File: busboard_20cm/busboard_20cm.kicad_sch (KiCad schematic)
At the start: 20 parts, among them J101 Conn_02x03_Odd_Even, J102 Conn_02x03_Odd_Even, J103 Conn_02x08_Odd_Even, J104 Conn_02x08_Odd_Even, J105 Conn_02x08_Odd_Even, J106 Conn_02x08_Odd_Even, J107 Conn_02x08_Odd_Even, J108 Conn_02x08_Odd_Even, J109 Conn_02x08_Odd_Even, J110 Conn_02x08_Odd_Even, J111 Conn_02x08_Odd_Even, J112 Conn_02x08_Odd_Even

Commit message: other connectors
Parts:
- J101, J102: footprint Connector_Molex:Molex_Mega-Fit_76825-0006_2x03_P5.70mm_Horizontal -> Connector_Molex:Molex_Mini-Fit_Jr_5569-06A2_2x03_P4.20mm_Horizontal
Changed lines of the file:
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@@
     (property "Reference" "J102" (id 0) (at 80.01 39.37 0))
     (property "Value" "Conn_02x03_Odd_Even" (id 1) (at 80.01 41.91 0))
-    (property "Footprint" "Connector_Molex:Molex_Mega-Fit_76825-0006_2x03_P5.70mm_Horizontal" (id 2) (at 78.74 48.26 0)
+    (property "Footprint" "Connector_Molex:Molex_Mini-Fit_Jr_5569-06A2_2x03_P4.20mm_Horizontal" (id 2) (at 78.74 48.26 0)
       (effects (font (size 1.27 1.27)) hide)
     )
@@
     (property "Reference" "J101" (id 0) (at 57.15 39.37 0))
     (property "Value" "Conn_02x03_Odd_Even" (id 1) (at 57.15 41.91 0))
-    (property "Footprint" "Connector_Molex:Molex_Mega-Fit_76825-0006_2x03_P5.70mm_Horizontal" (id 2) (at 55.88 48.26 0)
+    (property "Footprint" "Connector_Molex:Molex_Mini-Fit_Jr_5569-06A2_2x03_P4.20mm_Horizontal" (id 2) (at 55.88 48.26 0)
       (effects (font (size 1.27 1.27)) hide)
     )
@@
     )
     (path "/f35fa862-5295-4a1c-906a-148decc7486d"
-      (reference "J101") (unit 1) (value "Conn_02x03_Odd_Even") (footprint "Connector_Molex:Molex_Mega-Fit_76825-0006_2x03_P5.70mm_Horizontal")
+      (reference "J101") (unit 1) (value "Conn_02x03_Odd_Even") (footprint "Connector_Molex:Molex_Mini-Fit_Jr_5569-06A2_2x03_P4.20mm_Horizontal")
     )
     (path "/d8365a49-83a6-4f8a-b632-574f5a95010c"
-      (reference "J102") (unit 1) (value "Conn_02x03_Odd_Even") (footprint "Connector_Molex:Molex_Mega-Fit_76825-0006_2x03_P5.70mm_Horizontal")
+      (reference "J102") (unit 1) (value "Conn_02x03_Odd_Even") (footprint "Connector_Molex:Molex_Mini-Fit_Jr_5569-06A2_2x03_P4.20mm_Horizontal")
     )
     (path "/50a9fff8-aee7-4c81-892e-762262cca06d"

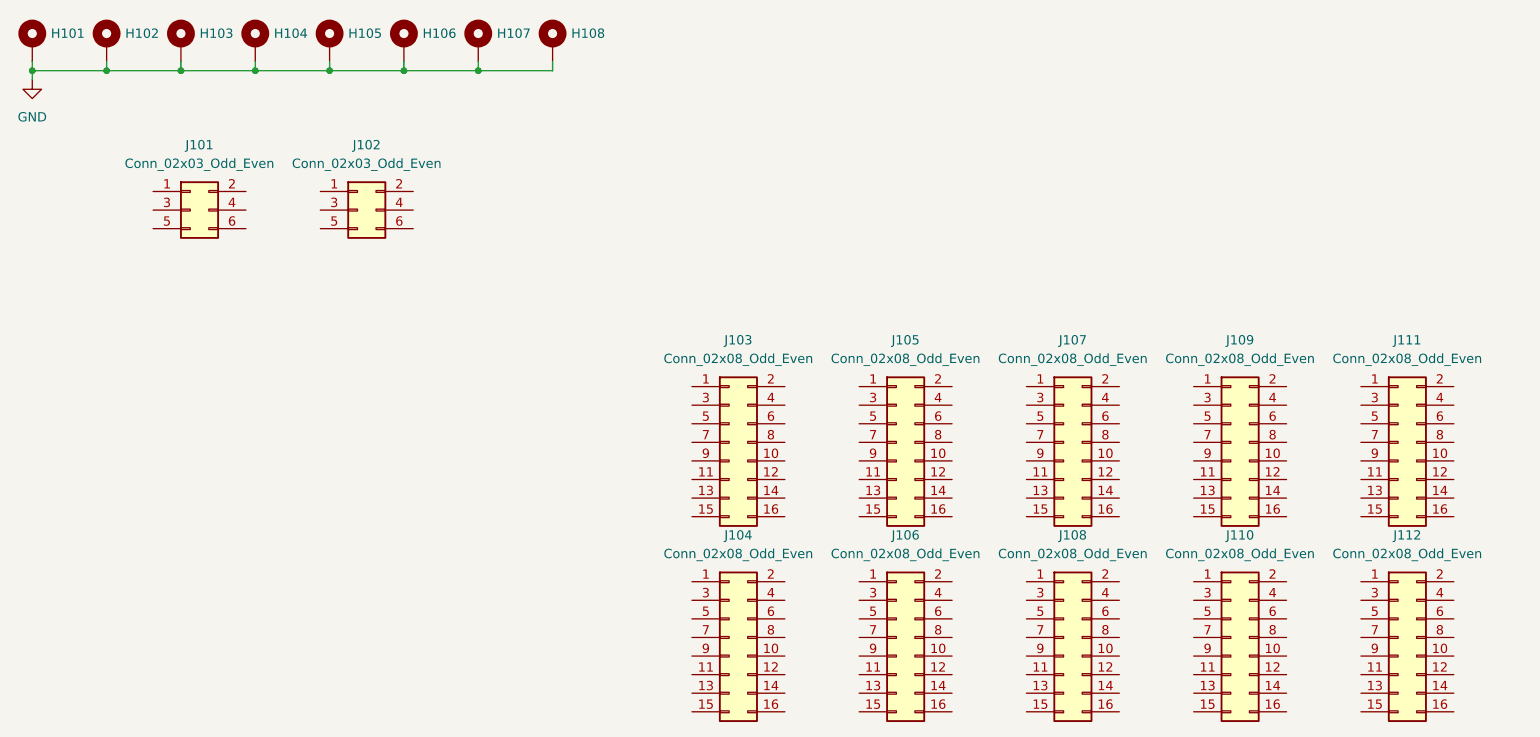
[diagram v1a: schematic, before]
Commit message: 20cm busboard PCB
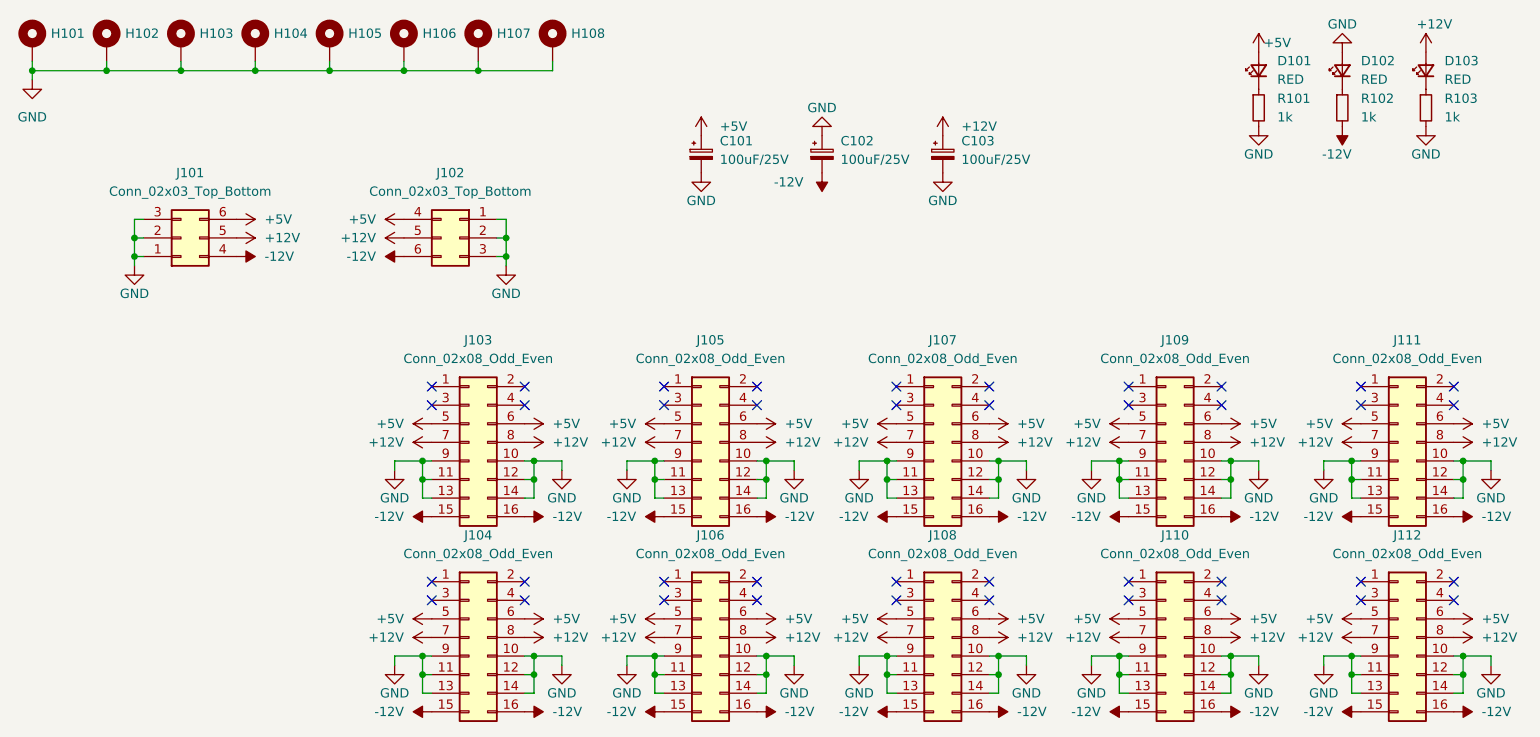
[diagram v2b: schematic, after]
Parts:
- removed J101, J102: Conn_02x03_Odd_Even, Connector_Molex:Molex_Mini-Fit_Jr_5569-06A2_2x03_P4.20mm_Horizontal, symbol Connector_Generic:Conn_02x03_Odd_Even
- added C101, C102, C103: 100uF/25V, Capacitor_SMD:CP_Elec_6.3x7.7, symbol Device:C_Polarized_Small
- added D101, D102, D103: RED, LED_SMD:LED_0603_1608Metric, symbol Device:LED_Small
- added J101, J102: Conn_02x03_Top_Bottom, Connector_Molex:Molex_Mini-Fit_Jr_5569-06A2_2x03_P4.20mm_Horizontal, symbol Connector_Generic:Conn_02x03_Top_Bottom
- added R101, R102, R103: 1k, Resistor_SMD:R_0603_1608Metric, symbol Device:R_Small
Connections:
- net GND: now also J103.10 (Pin_10), J103.11 (Pin_11), J103.12 (Pin_12), J103.13 (Pin_13), J103.14 (Pin_14), J103.9 (Pin_9), J104.10 (Pin_10), J104.11 (Pin_11), J104.12 (Pin_12), J104.13 (Pin_13), J104.14 (Pin_14), J104.9 (Pin_9), J105.10 (Pin_10), J105.11 (Pin_11), J105.12 (Pin_12), J105.13 (Pin_13), J105.14 (Pin_14), J105.9 (Pin_9), J106.10 (Pin_10), J106.11 (Pin_11), J106.12 (Pin_12), J106.13 (Pin_13), J106.14 (Pin_14), J106.9 (Pin_9), J107.10 (Pin_10), J107.11 (Pin_11), J107.12 (Pin_12), J107.13 (Pin_13), J107.14 (Pin_14), J107.9 (Pin_9), J108.10 (Pin_10), J108.11 (Pin_11), J108.12 (Pin_12), J108.13 (Pin_13), J108.14 (Pin_14), J108.9 (Pin_9), J109.10 (Pin_10), J109.11 (Pin_11), J109.12 (Pin_12), J109.13 (Pin_13), J109.14 (Pin_14), J109.9 (Pin_9), J110.10 (Pin_10), J110.11 (Pin_11), J110.12 (Pin_12), J110.13 (Pin_13), J110.14 (Pin_14), J110.9 (Pin_9), J111.10 (Pin_10), J111.11 (Pin_11), J111.12 (Pin_12), J111.13 (Pin_13), J111.14 (Pin_14), J111.9 (Pin_9), J112.10 (Pin_10), J112.11 (Pin_11), J112.12 (Pin_12), J112.13 (Pin_13), J112.14 (Pin_14), J112.9 (Pin_9), C101.2, C102.1, C103.2, D102.2 (A), J101.1 (Pin_1), J101.2 (Pin_2), J101.3 (Pin_3), J102.1 (Pin_1), J102.2 (Pin_2), J102.3 (Pin_3), R101.2, R103.2
- net -12V: now reaches J112.15 (Pin_15)
- net -12V: now also J103.15 (Pin_15), J103.16 (Pin_16), J104.15 (Pin_15), J104.16 (Pin_16), J105.15 (Pin_15), J105.16 (Pin_16), J106.15 (Pin_15), J106.16 (Pin_16), J107.15 (Pin_15), J107.16 (Pin_16), J108.15 (Pin_15), J108.16 (Pin_16), J109.15 (Pin_15), J109.16 (Pin_16), J110.15 (Pin_15), J110.16 (Pin_16), J111.15 (Pin_15), J111.16 (Pin_16), J112.16 (Pin_16), C102.2, J101.4 (Pin_4), J102.6 (Pin_6), R102.2
- net +5V: now reaches J112.5 (Pin_5)
- net +5V: now also J103.5 (Pin_5), J103.6 (Pin_6), J104.5 (Pin_5), J104.6 (Pin_6), J105.5 (Pin_5), J105.6 (Pin_6), J106.5 (Pin_5), J106.6 (Pin_6), J107.5 (Pin_5), J107.6 (Pin_6), J108.5 (Pin_5), J108.6 (Pin_6), J109.5 (Pin_5), J109.6 (Pin_6), J110.5 (Pin_5), J110.6 (Pin_6), J111.5 (Pin_5), J111.6 (Pin_6), J112.6 (Pin_6), C101.1, D101.2 (A), J101.6 (Pin_6), J102.4 (Pin_4)
- net +12V: now reaches J112.7 (Pin_7)
- net +12V: now also J103.7 (Pin_7), J103.8 (Pin_8), J104.7 (Pin_7), J104.8 (Pin_8), J105.7 (Pin_7), J105.8 (Pin_8), J106.7 (Pin_7), J106.8 (Pin_8), J107.7 (Pin_7), J107.8 (Pin_8), J108.7 (Pin_7), J108.8 (Pin_8), J109.7 (Pin_7), J109.8 (Pin_8), J110.7 (Pin_7), J110.8 (Pin_8), J111.7 (Pin_7), J111.8 (Pin_8), J112.8 (Pin_8), C103.1, D103.2 (A), J101.5 (Pin_5), J102.5 (Pin_5)
- new net: D103.1 (K), R103.1
- new net: D102.1 (K), R102.1
- new net: D101.1 (K), R101.1
- no-connect marks 0 -> 40
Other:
- moved on the sheet: J103, J104, J105, J106, J107, J108, J109, J110
